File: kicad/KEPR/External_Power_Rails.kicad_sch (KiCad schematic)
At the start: 18 parts, among them J1 PINHD_1x20_Male, J12 PINHD_1x20_Male, J13 PINHD_1x20_Male, J14 PINHD_2x3_Male, J15 PINHD_1x10_Male, J16 PINHD_1x10_Male, J17 PINHD_1x20_Male, J18 PINHD_1x20_Male, J19 PINHD_1x20_Male, J2 PINHD_1x20_Male, J20 PINHD_1x20_Male, J21 PINHD_1x10_Male, J23 PINHD_1x10_Male, J24 PINHD_2x3_Male, J25 PINHD_2x3_Male, J26 PINHD_2x3_Male, J27 PINHD_2x3_Male, J30 PINHD_2x3_Male

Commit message: Adicionado conversores DC-DC e Logo da Rapport
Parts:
- added J22: Barrel_Jack, Barrel Jack:BarrelJack_Horizontal, symbol Connector:Barrel_Jack
- added PS1: TDN5-2410WISM, TDN 5WISM Series, 5 Watt:CONV_TDN5-2411WISM, symbol DC-DC Converters Traco Power:TDN5-2410WI
- added PS2: TDN5-2411WISM, TDN 5WISM Series, 5 Watt:CONV_TDN5-2411WISM, symbol DC-DC Converters Traco Power TDN5-2411WI:TDN5-2411WISM
- added PS3: TDN_5-2412WISM, TDN 5WISM Series, 5 Watt:CONV_TDN5-2411WISM, symbol DC-DC Converters Traco Power TDN5-2412WI:TDN_5-2412WISM
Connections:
- net +12V: now also PS3.7 (+VOUT)
- net +3.3V: now also PS1.7 (+VOUT)
- net +5V: now also PS2.7 (+VOUT)
- net GND: now also J22.2, PS1.2 (-VIN(GND)), PS1.6 (-VOUT), PS2.2 (-VIN(GND)), PS2.6 (-VOUT), PS3.2 (-VIN(GND)), PS3.6 (-VOUT)
- new net +24V: J22.1, PS1.1 (+VIN(VCC)), PS2.1 (+VIN(VCC)), PS3.1 (+VIN(VCC))
- new net UCE_MCU_VCTL_12v: PS3.4 (ON/OFF)
- new net UCE_MCU_VCTL_3v3: PS1.4 (ON/OFF)
- new net UCE_MCU_VCTL_5V: PS2.4 (ON/OFF)
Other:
- title: (none) -> KEPR - Externals Power Rails

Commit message: Diversos ajustes no Power Rail
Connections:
- net +12V: no longer PS3.7 (+VOUT)
- net +3.3V: no longer PS1.7 (+VOUT)
- net +5V: no longer PS2.7 (+VOUT)
- net GND: now also PS1.5 (NC), PS2.5 (NC), PS3.5 (NC)
- new net +12v Shunt: PS3.7 (+VOUT)
- new net +3v3 Shunt: PS1.7 (+VOUT)
- new net +5v Shunt: PS2.7 (+VOUT)
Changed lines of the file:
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@@
 	)
 	(junction
+		(at 101.6 177.8)
+		(diameter 0)
+		(color 0 0 0 0)
+	)
+	(junction
 		(at 160.02 91.44)
 		(diameter 0)
@@
 	)
 	(junction
+		(at 101.6 144.78)
+		(diameter 0)
+		(color 0 0 0 0)
+	)
+	(junction
 		(at 226.06 127)
 		(diameter 0)
@@
 	)
 	(junction
+		(at 101.6 114.3)
+		(diameter 0)
+		(color 0 0 0 0)
+	)
+	(junction
 		(at 243.84 83.82)
 		(diameter 0)
@@
 	(wire
 		(pts
-			(xy 101.6 114.3) (xy 109.22 114.3)
-		)
-		(stroke
-			(width 0)
-			(type default)
-		)
-	)
-	(wire
-		(pts
 			(xy 109.22 69.85) (xy 109.22 71.12)
 		)
@@
 	(wire
 		(pts
+			(xy 101.6 109.22) (xy 101.6 114.3)
+		)
+		(stroke
+			(width 0)
+			(type default)
+		)
+	)
+	(wire
+		(pts
 			(xy 227.33 167.64) (xy 227.33 170.18)
 		)
@@
 	(wire
 		(pts
+			(xy 101.6 172.72) (xy 101.6 177.8)
+		)
+		(stroke
+			(width 0)
+			(type default)
+		)
+	)
+	(wire
+		(pts
 			(xy 193.04 121.92) (xy 196.85 121.92)
 		)
@@
 	(wire
 		(pts
+			(xy 101.6 139.7) (xy 101.6 144.78)
+		)
+		(stroke
+			(width 0)
+			(type default)
+		)
+	)
+	(wire
+		(pts
 			(xy 66.04 114.3) (xy 40.64 114.3)
 		)
@@
 	(wire
 		(pts
-			(xy 121.92 167.64) (xy 101.6 167.64)
+			(xy 114.3 167.64) (xy 101.6 167.64)
 		)
 		(stroke
@@
 	(wire
 		(pts
-			(xy 106.68 101.6) (xy 106.68 104.14)
+			(xy 109.22 101.6) (xy 109.22 104.14)
 		)
 		(stroke
@@
 	(wire
 		(pts
+			(xy 101.6 114.3) (xy 109.22 114.3)
+		)
+		(stroke
+			(width 0)
+			(type default)
+		)
+	)
+	(wire
+		(pts
 			(xy 129.54 119.38) (xy 129.54 116.84)
 		)
@@
 	(wire
 		(pts
-			(xy 114.3 134.62) (xy 101.6 134.62)
+			(xy 111.76 134.62) (xy 101.6 134.62)
 		)
 		(stroke
@@
 	(wire
 		(pts
-			(xy 114.3 101.6) (xy 114.3 134.62)
+			(xy 111.76 101.6) (xy 111.76 134.62)
 		)
 		(stroke
@@
 	(wire
 		(pts
-			(xy 106.68 104.14) (xy 101.6 104.14)
+			(xy 109.22 104.14) (xy 101.6 104.14)
 		)
 		(stroke
@@
 	(wire
 		(pts
-			(xy 121.92 101.6) (xy 121.92 167.64)
+			(xy 114.3 101.6) (xy 114.3 167.64)
 		)
 		(stroke
@@
 		)
 	)
+	(global_label "+12v Shunt"
+		(shape input)
+		(at 114.3 101.6 90)
+		(fields_autoplaced yes)
+		(effects
+			(font
+				(size 1.27 1.27)
+			)
+			(justify left)
+		)
+		(property "Intersheetrefs" "${INTERSHEET_REFS}"
+			(at 114.3 87.306 90)
+			(effects
+				(font
+					(size 1.27 1.27)
+				)
+				(justify left)
+				(hide yes)
+			)
+		)
+	)
+	(global_label "+3v3 Shunt"
+		(shape input)
+		(at 109.22 101.6 90)
+		(fields_autoplaced yes)
+		(effects
+			(font
+				(size 1.27 1.27)
+			)
+			(justify left)
+		)
+		(property "Intersheetrefs" "${INTERSHEET_REFS}"
+			(at 109.22 87.306 90)
+			(effects
+				(font
+					(size 1.27 1.27)
+				)
+				(justify left)
+				(hide yes)
+			)
+		)
+	)
+	(global_label "+5v Shunt"
+		(shape input)
+		(at 111.76 101.6 90)
+		(fields_autoplaced yes)
+		(effects
+			(font
+				(size 1.27 1.27)
+			)
+			(justify left)
+		)
+		(property "Intersheetrefs" "${INTERSHEET_REFS}"
+			(at 111.76 88.5155 90)
+			(effects
+				(font
+					(size 1.27 1.27)
+				)
+				(justify left)
+				(hide yes)
+			)
+		)
+	)
 	(symbol
 		(lib_id "power:+12V")
@@
 	)
 	(symbol
-		(lib_id "power:+5V")
-		(at 114.3 101.6 0)
-		(unit 1)
-		(exclude_from_sim no)
-		(in_bom yes)
-		(on_board yes)
-		(dnp no)
-		(fields_autoplaced yes)
-		(property "Reference" "#PWR030"
-			(at 114.3 105.41 0)
-			(effects
-				(font
-					(size 1.27 1.27)
-				)
-				(hide yes)
-			)
-		)
-		(property "Value" "+5V"
-			(at 114.3 96.52 0)
-			(effects
-				(font
-					(size 1.27 1.27)
-				)
-			)
-		)
-		(property "Footprint" ""
-			(at 114.3 101.6 0)
-			(effects
-				(font
-					(size 1.27 1.27)
-				)
-				(hide yes)
-			)
-		)
-		(property "Datasheet" ""
-			(at 114.3 101.6 0)
-			(effects
-				(font
-					(size 1.27 1.27)
-				)
-				(hide yes)
-			)
-		)
-		(property "Description" "Power symbol creates a global label with name \"+5V\""
-			(at 114.3 101.6 0)
-			(effects
-				(font
-					(size 1.27 1.27)
-				)
-				(hide yes)
-			)
-		)
-		(pin "1"
-		)
-		(instances
-			(project "KEPR"
-				(path "/5d9e1dfb-5ec5-4e06-bbdb-9cbfa1c0b9f1/51ee32d1-fe48-4676-ab84-bc891947886f/4741b4dc-2a05-46d3-a722-9e7e2f449984"
-					(reference "#PWR030")
-					(unit 1)
-				)
-			)
-		)
-	)
-	(symbol
 		(lib_id "power:+3.3V")
 		(at 181.61 68.58 0)
@@
 	)
 	(symbol
-		(lib_id "power:+12V")
-		(at 121.92 101.6 0)
-		(unit 1)
-		(exclude_from_sim no)
-		(in_bom yes)
-		(on_board yes)
-		(dnp no)
-		(fields_autoplaced yes)
-		(property "Reference" "#PWR023"
-			(at 121.92 105.41 0)
-			(effects
-				(font
-					(size 1.27 1.27)
-				)
-				(hide yes)
-			)
-		)
-		(property "Value" "+12V"
-			(at 121.92 96.52 0)
-			(effects
-				(font
-					(size 1.27 1.27)
-				)
-			)
-		)
-		(property "Footprint" ""
-			(at 121.92 101.6 0)
-			(effects
-				(font
-					(size 1.27 1.27)
-				)
-				(hide yes)
-			)
-		)
-		(property "Datasheet" ""
-			(at 121.92 101.6 0)
-			(effects
-				(font
-					(size 1.27 1.27)
-				)
-				(hide yes)
-			)
-		)
-		(property "Description" "Power symbol creates a global label with name \"+12V\""
-			(at 121.92 101.6 0)
-			(effects
-				(font
-					(size 1.27 1.27)
-				)
-				(hide yes)
-			)
-		)
-		(pin "1"
-		)
-		(instances
-			(project "KEPR"
-				(path "/5d9e1dfb-5ec5-4e06-bbdb-9cbfa1c0b9f1/51ee32d1-fe48-4676-ab84-bc891947886f/4741b4dc-2a05-46d3-a722-9e7e2f449984"
-					(reference "#PWR023")
-					(unit 1)
-				)
-			)
-		)
-	)
-	(symbol
 		(lib_id "power:+24V")
 		(at 35.56 96.52 0)
@@
 					(unit 1)
 				)
-			)
-		)
-	)
-	(symbol
-		(lib_id "power:+3.3V")
-		(at 106.68 101.6 0)
-		(unit 1)
-		(exclude_from_sim no)
-		(in_bom yes)
-		(on_board yes)
-		(dnp no)
-		(fields_autoplaced yes)
-		(property "Reference" "#PWR031"
-			(at 106.68 105.41 0)
-			(effects
-				(font
-					(size 1.27 1.27)
-				)
-				(hide yes)
-			)
-		)
-		(property "Value" "+3.3V"
-			(at 106.68 96.52 0)
-			(effects
-				(font
-					(size 1.27 1.27)
-				)
-			)
-		)
-		(property "Footprint" ""
-			(at 106.68 101.6 0)
-			(effects
-				(font
-					(size 1.27 1.27)
-				)
-				(hide yes)
-			)
-		)
-		(property "Datasheet" ""
-			(at 106.68 101.6 0)
-			(effects
-				(font
-					(size 1.27 1.27)
-				)
-				(hide yes)
-			)
-		)
-		(property "Description" "Power symbol creates a global label with name \"+3.3V\""
-			(at 106.68 101.6 0)
-			(effects
-				(font
-					(size 1.27 1.27)
-				)
-				(hide yes)
-			)
-		)
-		(pin "1"
-		)
-		(instances
-			(project "KEPR"
-				(path "/5d9e1dfb-5ec5-4e06-bbdb-9cbfa1c0b9f1/51ee32d1-fe48-4676-ab84-bc891947886f/4741b4dc-2a05-46d3-a722-9e7e2f449984"
-					(reference "#PWR031")
-					(unit 1)
-				)

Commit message: Ajustes no Power Rail, entre outros ajustes.
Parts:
- removed J13, J18, J2, J20: PINHD_1x20_Male, Connector_PinHeader_2.54mm:PinHeader_1x20_P2.54mm_Vertical, symbol PCM_SL_Pin_Headers:PINHD_1x20_Male
- removed J14, J25, J27: PINHD_2x3_Male, Connector_PinHeader_2.54mm:PinHeader_2x03_P2.54mm_Vertical, symbol PCM_SL_Pin_Headers:PINHD_2x3_Male
- removed J15, J21: PINHD_1x10_Male, Connector_PinHeader_2.54mm:PinHeader_1x10_P2.54mm_Vertical, symbol PCM_SL_Pin_Headers:PINHD_1x10_Male
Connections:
- net Vout_external_3: now reaches J16.1, J16.10, J16.2, J16.3, J16.4, J16.5, J16.6, J16.7, J16.8, J16.9, J30.1, J30.3, J30.5
- net Vout_external_2: now reaches J12.1, J12.10, J12.11, J12.12, J12.13, J12.14, J12.15, J12.16, J12.17, J12.18, J12.19, J12.2, J12.20, J12.3, J12.4, J12.5, J12.6, J12.7, J12.8, J12.9, J26.1, J26.3, J26.5
- net Vout_external_1: now reaches J1.1, J1.10, J1.11, J1.12, J1.13, J1.14, J1.15, J1.16, J1.17, J1.18, J1.19, J1.2, J1.20, J1.3, J1.4, J1.5, J1.6, J1.7, J1.8, J1.9, J24.1, J24.3, J24.5

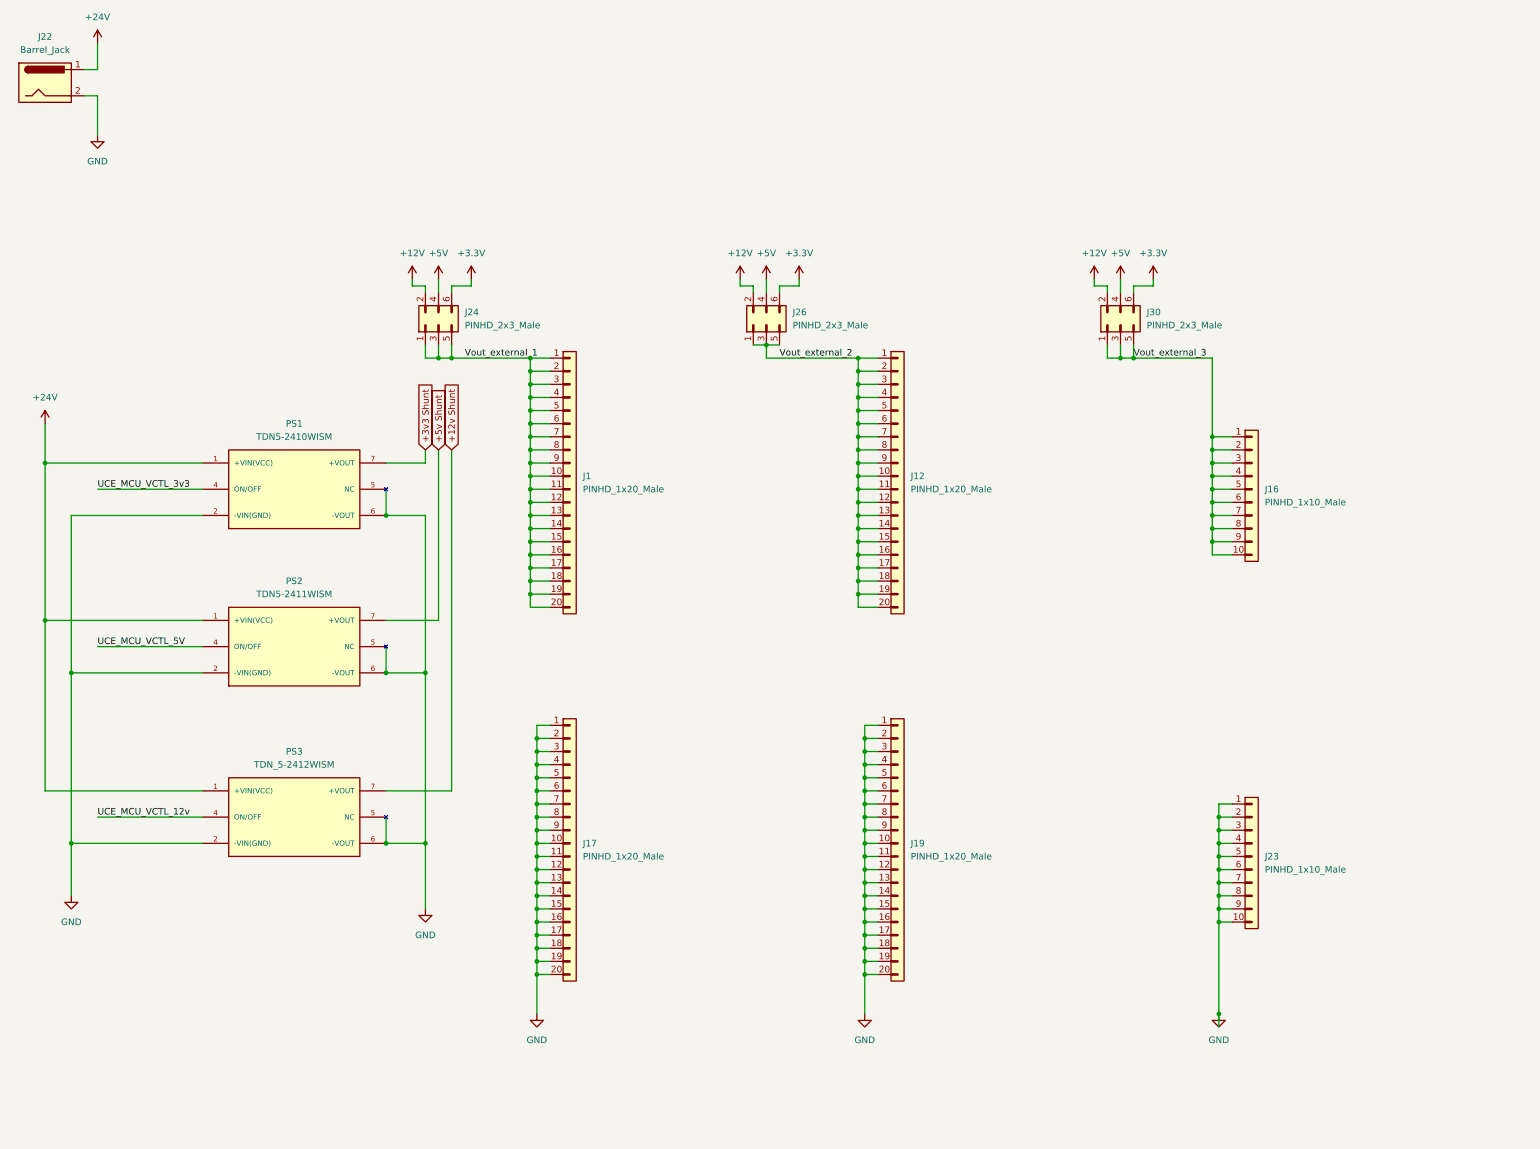
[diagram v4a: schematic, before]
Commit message: Iniciado a distribuição das vias.
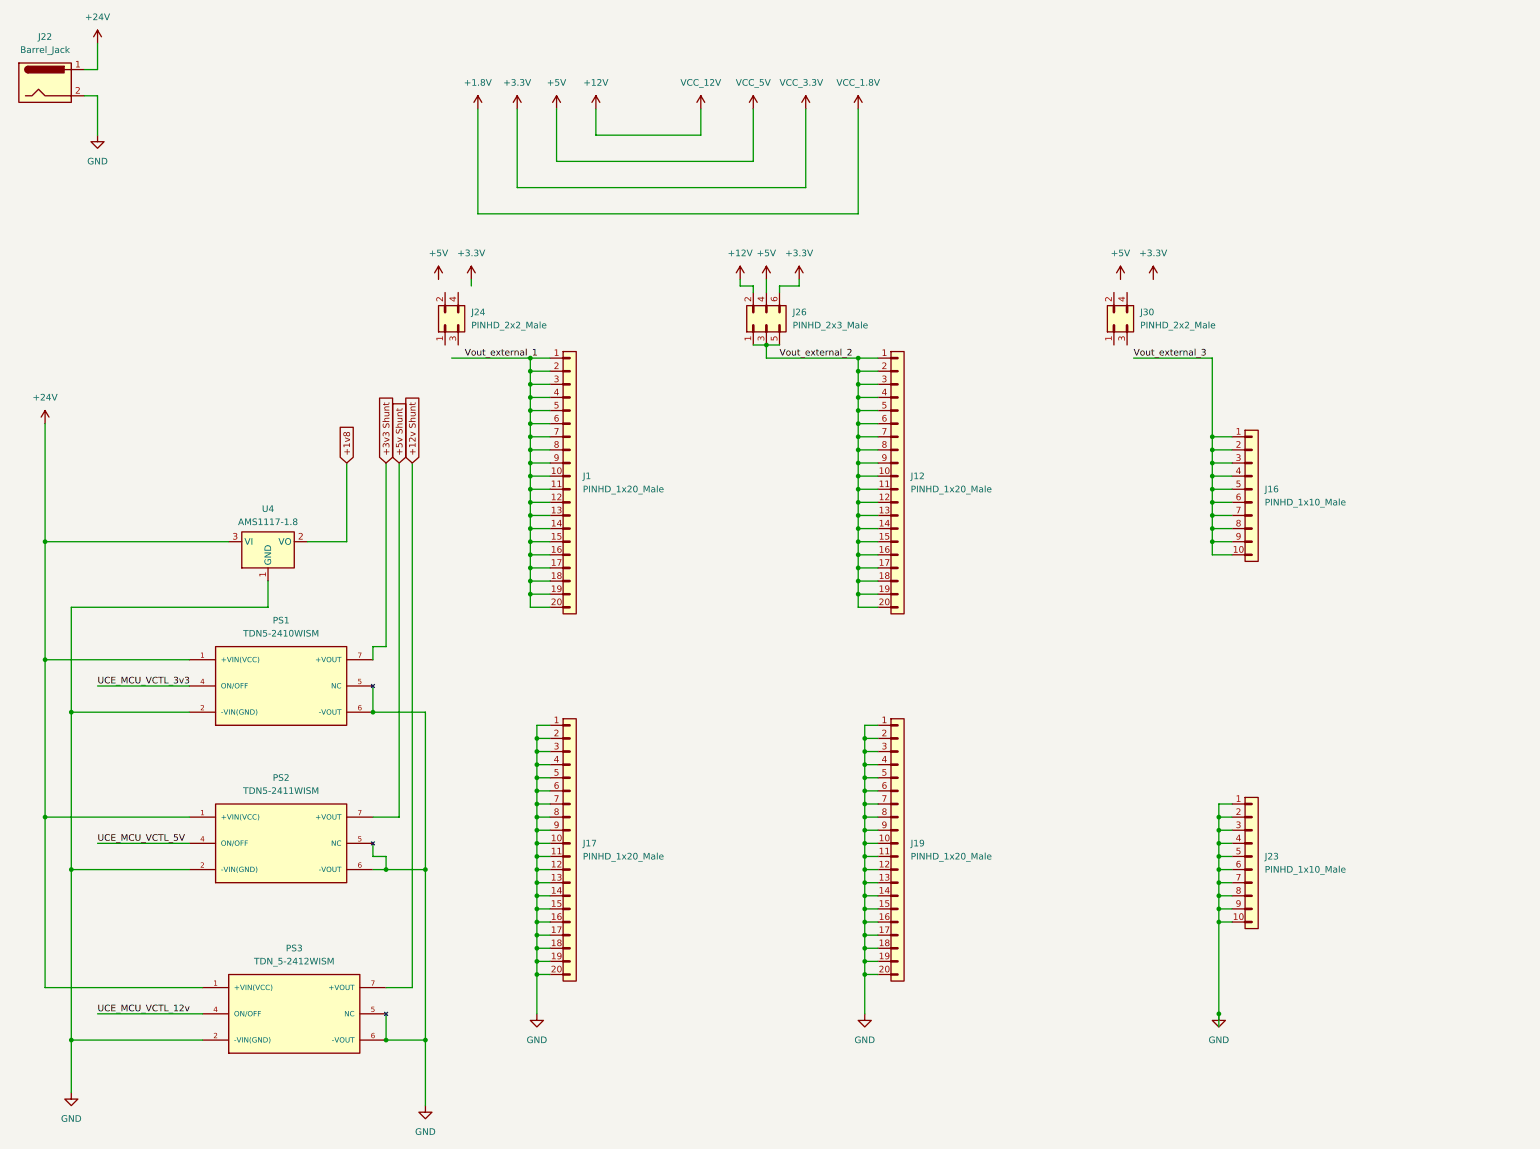
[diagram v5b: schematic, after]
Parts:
- removed J24, J30: PINHD_2x3_Male, Connector_PinHeader_2.54mm:PinHeader_2x03_P2.54mm_Vertical, symbol PCM_SL_Pin_Headers:PINHD_2x3_Male
- added J24, J30: PINHD_2x2_Male, Connector_PinHeader_2.54mm:PinHeader_2x02_P2.54mm_Vertical, symbol PCM_SL_Pin_Headers:PINHD_2x2_Male
- added U4: AMS1117-1.8, Package_TO_SOT_SMD:SOT-223-3_TabPin2, symbol Regulator_Linear:AMS1117-1.8
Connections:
- net +24V: now also U4.3 (VI)
- net GND: now also U4.1 (GND)
- new net +1v8: U4.2 (VO)
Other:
- moved on the sheet: PS1, PS2, PS3

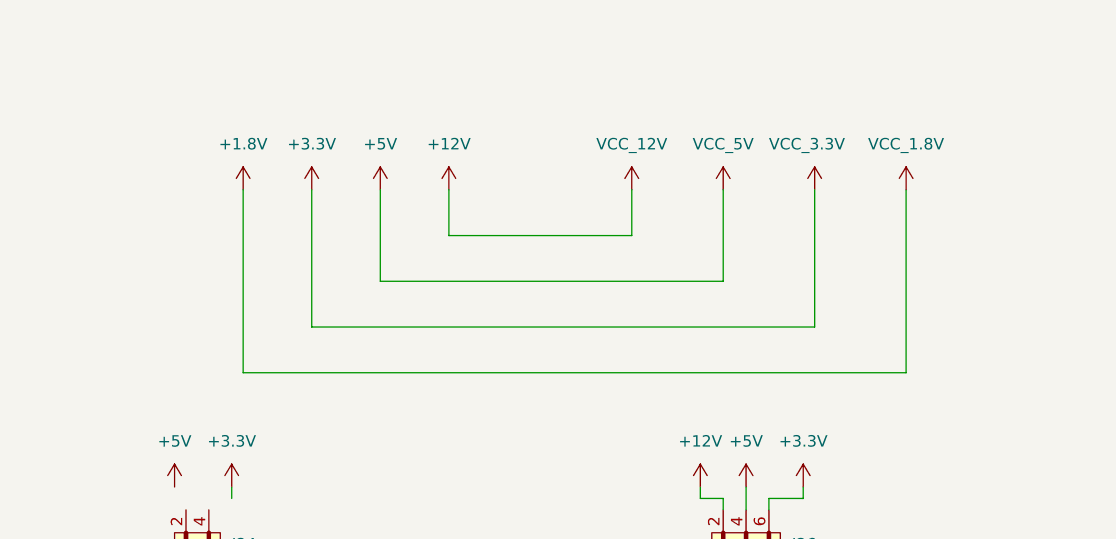
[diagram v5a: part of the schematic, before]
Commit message: Diversos ajustes no barramento e ampliação das trilhas na PCB
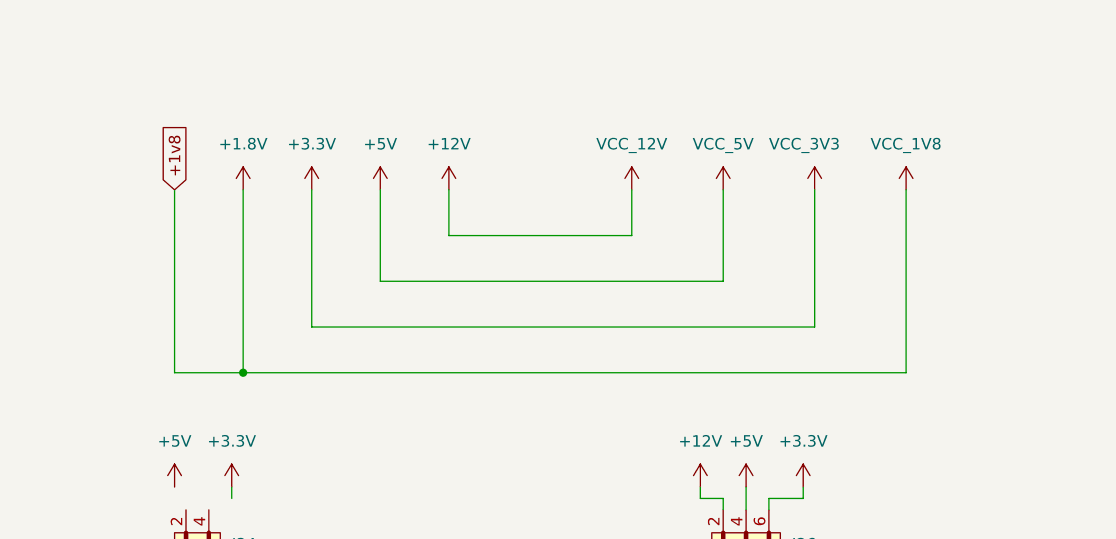
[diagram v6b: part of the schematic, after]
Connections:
- net +1v8 is gone; now on net +1.8V: U4.2 (VO)
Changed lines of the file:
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@@
 	)
 	(junction
+		(at 119.38 55.88)
+		(diameter 0)
+		(color 0 0 0 0)
+	)
+	(junction
 		(at 193.04 99.06)
 		(diameter 0)
@@
 	(wire
 		(pts
+			(xy 111.76 35.56) (xy 111.76 55.88)
+		)
+		(stroke
+			(width 0)
+			(type default)
+		)
+	)
+	(wire
+		(pts
 			(xy 99.06 139.7) (xy 99.06 142.24)
 		)
@@
 	(wire
 		(pts
+			(xy 119.38 55.88) (xy 193.04 55.88)
+		)
+		(stroke
+			(width 0)
+			(type default)
+		)
+	)
+	(wire
+		(pts
 			(xy 172.72 35.56) (xy 172.72 45.72)
 		)
@@
 	(wire
 		(pts
-			(xy 130.81 154.94) (xy 130.81 157.48)
+			(xy 111.76 55.88) (xy 119.38 55.88)
 		)
 		(stroke
@@
 	(wire
 		(pts
-			(xy 127 50.8) (xy 182.88 50.8)
+			(xy 130.81 154.94) (xy 130.81 157.48)
 		)
 		(stroke
@@
 	(wire
 		(pts
-			(xy 129.54 99.06) (xy 133.35 99.06)
+			(xy 127 50.8) (xy 182.88 50.8)
 		)
 		(stroke
@@
 	(wire
 		(pts
-			(xy 194.31 157.48) (xy 194.31 160.02)
+			(xy 129.54 99.06) (xy 133.35 99.06)
 		)
 		(stroke
@@
 	(wire
 		(pts
-			(xy 193.04 121.92) (xy 193.04 119.38)
+			(xy 194.31 157.48) (xy 194.31 160.02)
 		)
 		(stroke
@@
 	(wire
 		(pts
-			(xy 193.04 55.88) (xy 119.38 55.88)
+			(xy 193.04 121.92) (xy 193.04 119.38)
 		)
 		(stroke
@@
 		)
 	)
+	(global_label "+1v8"
+		(shape input)
+		(at 111.76 35.56 90)
+		(fields_autoplaced yes)
+		(effects
+			(font
+				(size 1.27 1.27)
+			)
+			(justify left)
+		)
+		(property "Intersheetrefs" "${INTERSHEET_REFS}"
+			(at 111.76 27.6158 90)
+			(effects
+				(font
+					(size 1.27 1.27)
+				)
+				(justify left)
+				(hide yes)
+			)
+		)
+	)
 	(global_label "+12v Shunt"
 		(shape input)
@@
 		(at 114.3 76.2 90)
 		(unit 1)
-		(exclude_from_sim no)
+		(exclude_from_sim yes)
 		(in_bom yes)
 		(on_board yes)
@@
 			)
 		)
-		(property "Value" "VCC_3.3V"
+		(property "Value" "VCC_3V3"
 			(at 177.8 30.48 0)
 			(effects
@@
 			)
 		)
-		(property "Value" "VCC_1.8V"
+		(property "Value" "VCC_1V8"
 			(at 193.04 30.48 0)
 			(effects
